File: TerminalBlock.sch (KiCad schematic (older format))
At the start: 2 parts, among them P4 12 Pin Terminal Block, P5 3 Pin TB

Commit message: Layout Work Session 14 Output
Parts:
- added C26, C27, C28, C29: C, SM1210, symbol C
- added R56: R, SM0805, symbol R
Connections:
- net +3.3V: now also C27.1
- net +5P: now also C26.1
- net GND_PWR: now also C26.2, C27.2, C28.2, C29.2, R56.1
- net TACH_IN: now also R56.2
- net V+_ADJ: now also C29.1
- net V-_ADJ: now also C28.1
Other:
- moved on the sheet: P4
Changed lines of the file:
@@
-EESchema Schematic File Version 2  date 11/21/2013 11:46:41 PM
+EESchema Schematic File Version 2  date 11/24/2013 3:13:43 PM
 LIBS:power
 LIBS:device
@@
 Sheet 7 9
 Title ""
-Date "22 nov 2013"
+Date "24 nov 2013"
 Rev ""
 Comp ""
@@
 RELAY_NC
 $Comp
-L +3.3V #PWR037
+L +3.3V #PWR43
 U 1 1 523FFDA7
 P 750 3500
-F 0 "#PWR037" H 750 3460 30  0001 C CNN
+F 0 "#PWR43" H 750 3460 30  0001 C CNN
 F 1 "+3.3V" H 750 3610 30  0000 C CNN
 F 2 "~" H 750 3500 60  0000 C CNN
@@
 L CONN_12 P4
 U 1 1 5258A829
-P 5850 1450
-F 0 "P4" V 5800 1450 60  0000 C CNN
-F 1 "12 Pin Terminal Block" V 5900 1450 60  0000 C CNN
-F 2 "" H 5850 1450 60  0000 C CNN
-F 3 "" H 5850 1450 60  0000 C CNN
-F 4 "On Shore" H 5850 1450 60  0001 C CNN "MFG Name"
-F 5 "OSTTE120104" H 5850 1450 60  0001 C CNN "MFG Part Number"
-	1    5850 1450
+P 8100 1450
+F 0 "P4" V 8050 1450 60  0000 C CNN
+F 1 "12 Pin Terminal Block" V 8150 1450 60  0000 C CNN
+F 2 "" H 8100 1450 60  0000 C CNN
+F 3 "" H 8100 1450 60  0000 C CNN
+F 4 "On Shore" H 8100 1450 60  0001 C CNN "MFG Name"
+F 5 "OSTTE120104" H 8100 1450 60  0001 C CNN "MFG Part Number"
+	1    8100 1450
 	1    0    0    -1
 $EndComp
@@
 	2050 1350 2050 1000
 Wire Wire Line
-	2050 1000 5500 1000
-Wire Wire Line
-	2200 1100 5500 1100
+	2050 1000 7750 1000
+Wire Wire Line
+	2200 1100 7750 1100
 Wire Wire Line
 	2200 1100 2200 2150
@@
 	2350 1200 2350 2325
 Wire Wire Line
-	2350 1200 5500 1200
-Wire Wire Line
-	5500 1300 2500 1300
+	2350 1200 7750 1200
+Wire Wire Line
+	7750 1300 2500 1300
 Wire Wire Line
 	2500 1300 2500 2600
@@
 	2700 2825 2700 1400
 Wire Wire Line
-	2700 1400 5500 1400
+	2700 1400 7750 1400
 Wire Wire Line
 	1800 3350 3000 3350
@@
 	2850 1500 2850 3000
 Wire Wire Line
-	2850 1500 5500 1500
-Wire Wire Line
-	5500 1600 3000 1600
+	2850 1500 7750 1500
+Wire Wire Line
+	7750 1600 3000 1600
 Wire Wire Line
 	3000 1600 3000 3350
@@
 	3200 3600 3200 1700
 Wire Wire Line
-	3200 1700 5500 1700
-Wire Wire Line
-	5500 1800 3400 1800
+	3200 1700 7750 1700
+Wire Wire Line
+	7750 1800 3400 1800
 Wire Wire Line
 	3400 1800 3400 4100
@@
 	3550 4400 3550 1900
 Wire Wire Line
-	3550 1900 5500 1900
-Wire Wire Line
-	5500 2000 3750 2000
+	3550 1900 7750 1900
+Wire Wire Line
+	7750 2000 3750 2000
 Wire Wire Line
 	3750 2000 3750 4550
@@
 	1825 2825 2700 2825
 Wire Wire Line
-	1450 900  5500 900
-$Comp
-L GND_PWR #PWR038
+	1450 900  7750 900
+$Comp
+L GND_PWR #PWR44
 U 1 1 527EF77D
 P 1000 3875
-F 0 "#PWR038" H 1000 3875 30  0001 C CNN
+F 0 "#PWR44" H 1000 3875 30  0001 C CNN
 F 1 "GND_PWR" H 1000 3805 30  0000 C CNN
 F 2 "~" H 1000 3875 60  0000 C CNN
@@
 	1    0    0    -1
 $EndComp
+$Comp
+L R R56
+U 1 1 52915224
+P 6300 2450
+F 0 "R56" V 6380 2450 40  0000 C CNN
+F 1 "R" V 6307 2451 40  0000 C CNN
+F 2 "SM0805" V 6230 2450 30  0000 C CNN
+F 3 "~" H 6300 2450 30  0000 C CNN
+	1    6300 2450
+	1    0    0    1
+$EndComp
+$Comp
+L GND_PWR #PWR46
+U 1 1 52915231
+P 5650 3450
+F 0 "#PWR46" H 5650 3450 30  0001 C CNN
+F 1 "GND_PWR" H 5650 3380 30  0000 C CNN
+F 2 "~" H 5650 3450 60  0000 C CNN
+F 3 "~" H 5650 3450 60  0000 C CNN
+	1    5650 3450
+	1    0    0    -1
+$EndComp
+Wire Wire Line
+	6300 3200 6300 2700
+$Comp
+L C C29
+U 1 1 52915CE9
+P 5600 2500
+F 0 "C29" H 5600 2600 40  0000 L CNN
+F 1 "C" H 5606 2415 40  0000 L CNN
+F 2 "SM1210" H 5638 2350 30  0000 C CNN
+F 3 "~" H 5600 2500 60  0000 C CNN
+	1    5600 2500
+	1    0    0    -1
+$EndComp
+Wire Wire Line
+	6300 2200 6300 1100
+Connection ~ 6300 1100
+Wire Wire Line
+	4500 3200 6300 3200
+Wire Wire Line
+	5650 3200 5650 3450
+Wire Wire Line
+	5600 2700 5600 3200
+Connection ~ 5650 3200
+$Comp
+L C C28
+U 1 1 52915E58
+P 5250 2500
+F 0 "C28" H 5250 2600 40  0000 L CNN
+F 1 "C" H 5256 2415 40  0000 L CNN
+F 2 "SM1210" H 5288 2350 30  0000 C CNN
+F 3 "~" H 5250 2500 60  0000 C CNN
+	1    5250 2500
+	1    0    0    -1
+$EndComp
+$Comp
+L C C27
+U 1 1 52915E5E
+P 4900 2500
+F 0 "C27" H 4900 2600 40  0000 L CNN
+F 1 "C" H 4906 2415 40  0000 L CNN
+F 2 "SM1210" H 4938 2350 30  0000 C CNN
+F 3 "~" H 4900 2500 60  0000 C CNN
+	1    4900 2500
+	1    0    0    -1
+$EndComp
+$Comp
+L C C26
+U 1 1 52915E6E
+P 4500 2500
+F 0 "C26" H 4500 2600 40  0000 L CNN
+F 1 "C" H 4506 2415 40  0000 L CNN
+F 2 "SM1210" H 4538 2350 30  0000 C CNN
+F 3 "~" H 4500 2500 60  0000 C CNN
+	1    4500 2500
+	1    0    0    -1
+$EndComp
+Wire Wire Line
+	4500 2700 4500 3200
+Connection ~ 5600 3200
+Wire Wire Line
+	5250 2700 5250 3200
+Connection ~ 5250 3200
+Wire Wire Line
+	4900 2700 4900 3200
+Connection ~ 4900 3200
+Wire Wire Line
+	5600 2300 5600 2000
+Connection ~ 5600 2000
+Wire Wire Line
+	5250 2300 5250 1900
+Connection ~ 5250 1900
+Wire Wire Line
+	4900 2300 4900 1800
+Connection ~ 4900 1800
+Wire Wire Line
+	4500 2300 4500 1600
+Connection ~ 4500 1600
 $EndSCHEMATC

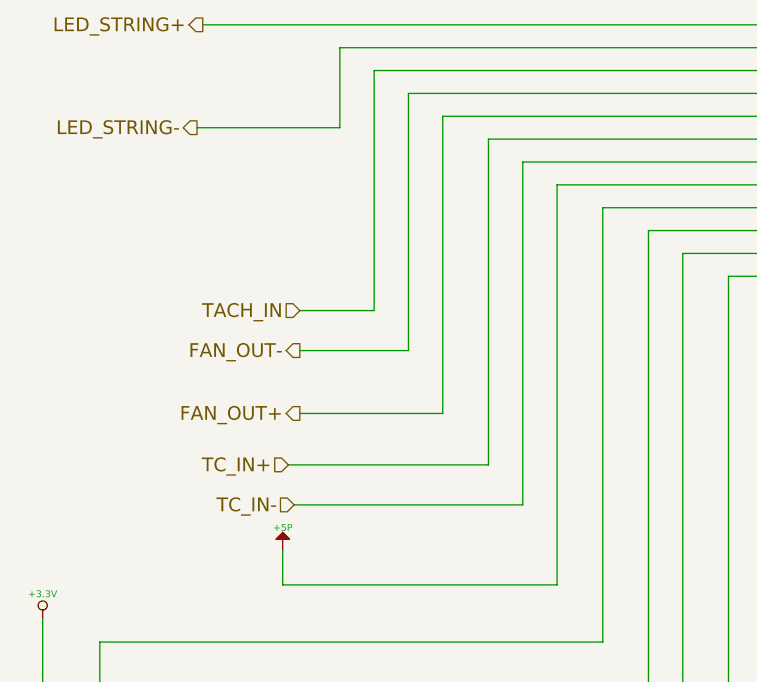
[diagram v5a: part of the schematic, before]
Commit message: Analog IO Cleanup/Additions
Added some placed holder caps and resistors
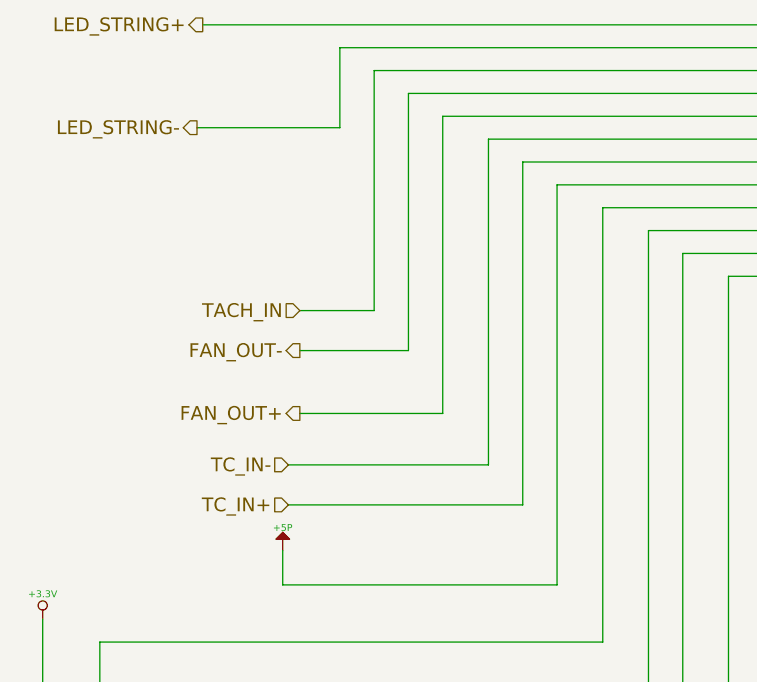
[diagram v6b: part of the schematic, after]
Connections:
- net TC_IN+: now also P4.7 (P7); no longer P4.6 (P6)
- net TC_IN-: now also P4.6 (P6); no longer P4.7 (P7)
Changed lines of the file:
@@
-EESchema Schematic File Version 2  date 12/18/2013 11:27:15 PM
+EESchema Schematic File Version 2  date 2/16/2014 3:41:32 PM
 LIBS:power
 LIBS:device
@@
 Sheet 7 9
 Title ""
-Date "19 dec 2013"
+Date "16 feb 2014"
 Rev ""
 Comp ""
@@
 Text HLabel 1425 1350 0    60   Output ~ 0
 LED_STRING-
+Text HLabel 1825 3000 0    60   Input ~ 0
+TC_IN+
 Text HLabel 1825 2825 0    60   Input ~ 0
-TC_IN+
-Text HLabel 1850 3000 0    60   Input ~ 0
 TC_IN-
 Text HLabel 2850 5500 0    60   BiDi ~ 0
@@
 RELAY_NC
 $Comp
-L +3.3V #PWR46
+L +3.3V #PWR040
 U 1 1 523FFDA7
 P 750 3500
-F 0 "#PWR46" H 750 3460 30  0001 C CNN
+F 0 "#PWR040" H 750 3460 30  0001 C CNN
 F 1 "+3.3V" H 750 3610 30  0000 C CNN
 F 2 "~" H 750 3500 60  0000 C CNN
@@
 	750  4100 3400 4100
 Wire Wire Line
-	2850 1500 2850 3000
+	2850 3000 2850 1500
 Wire Wire Line
 	2850 1500 7750 1500
@@
 	750  4100 750  3500
 Wire Wire Line
-	2850 3000 1850 3000
+	1825 3000 2850 3000
 Wire Wire Line
 	2350 2325 1875 2325
@@
 	1450 900  7750 900
 $Comp
-L GND_PWR #PWR47
+L GND_PWR #PWR041
 U 1 1 527EF77D
 P 1000 3875
-F 0 "#PWR47" H 1000 3875 30  0001 C CNN
+F 0 "#PWR041" H 1000 3875 30  0001 C CNN
 F 1 "GND_PWR" H 1000 3805 30  0000 C CNN
 F 2 "~" H 1000 3875 60  0000 C CNN
@@
 $EndComp
 $Comp
-L GND_PWR #PWR49
+L GND_PWR #PWR042
 U 1 1 52915231
 P 5650 3450
-F 0 "#PWR49" H 5650 3450 30  0001 C CNN
+F 0 "#PWR042" H 5650 3450 30  0001 C CNN
 F 1 "GND_PWR" H 5650 3380 30  0000 C CNN
 F 2 "~" H 5650 3450 60  0000 C CNN

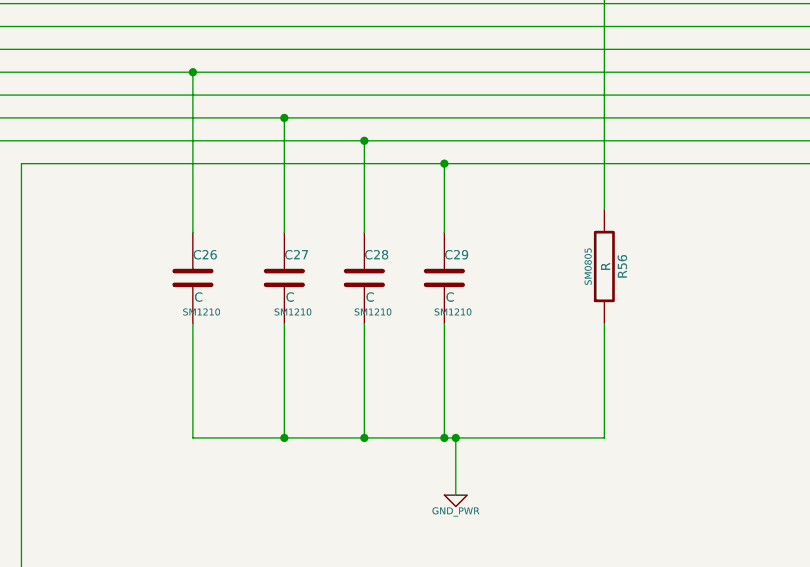
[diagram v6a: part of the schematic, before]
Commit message: Added Passive Values and SPICE models
As part of week 1 of Session 1B, we added a SPICE model of the In amp
and went through and assigned values to all of the passive components.
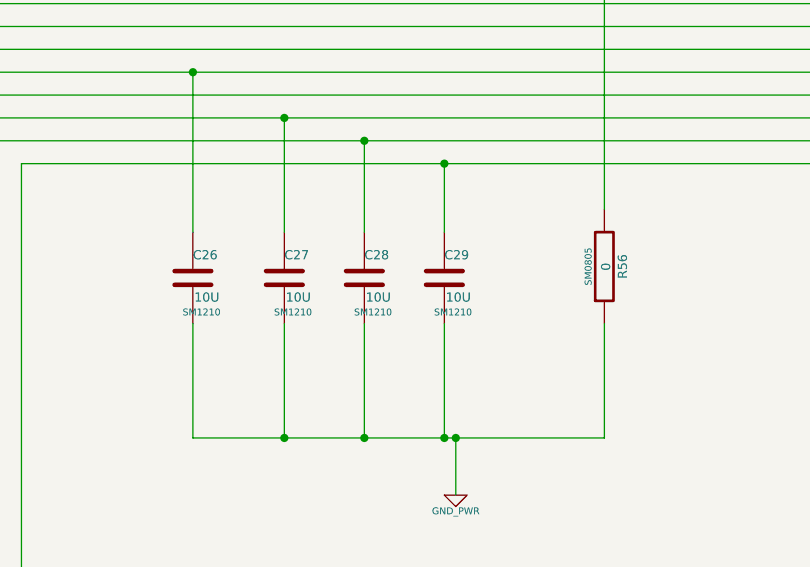
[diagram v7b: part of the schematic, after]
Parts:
- C26, C27, C28, C29: value C -> 10U
- R56: value R -> 0
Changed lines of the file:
@@
-EESchema Schematic File Version 2  date 2/16/2014 3:41:32 PM
+EESchema Schematic File Version 2  date 4/16/2014 11:04:06 PM
 LIBS:power
 LIBS:device
@@
 Sheet 7 9
 Title ""
-Date "16 feb 2014"
+Date "17 apr 2014"
 Rev ""
 Comp ""
@@
 P 6300 2450
 F 0 "R56" V 6380 2450 40  0000 C CNN
-F 1 "R" V 6307 2451 40  0000 C CNN
+F 1 "0" V 6307 2451 40  0000 C CNN
 F 2 "SM0805" V 6230 2450 30  0000 C CNN
 F 3 "~" H 6300 2450 30  0000 C CNN
@@
 P 5600 2500
 F 0 "C29" H 5600 2600 40  0000 L CNN
-F 1 "C" H 5606 2415 40  0000 L CNN
+F 1 "10U" H 5606 2415 40  0000 L CNN
 F 2 "SM1210" H 5638 2350 30  0000 C CNN
 F 3 "~" H 5600 2500 60  0000 C CNN
@@
 P 5250 2500
 F 0 "C28" H 5250 2600 40  0000 L CNN
-F 1 "C" H 5256 2415 40  0000 L CNN
+F 1 "10U" H 5256 2415 40  0000 L CNN
 F 2 "SM1210" H 5288 2350 30  0000 C CNN
 F 3 "~" H 5250 2500 60  0000 C CNN
@@
 P 4900 2500
 F 0 "C27" H 4900 2600 40  0000 L CNN
-F 1 "C" H 4906 2415 40  0000 L CNN
+F 1 "10U" H 4906 2415 40  0000 L CNN
 F 2 "SM1210" H 4938 2350 30  0000 C CNN
 F 3 "~" H 4900 2500 60  0000 C CNN
@@
 P 4500 2500
 F 0 "C26" H 4500 2600 40  0000 L CNN
-F 1 "C" H 4506 2415 40  0000 L CNN
+F 1 "10U" H 4506 2415 40  0000 L CNN
 F 2 "SM1210" H 4538 2350 30  0000 C CNN
 F 3 "~" H 4500 2500 60  0000 C CNN

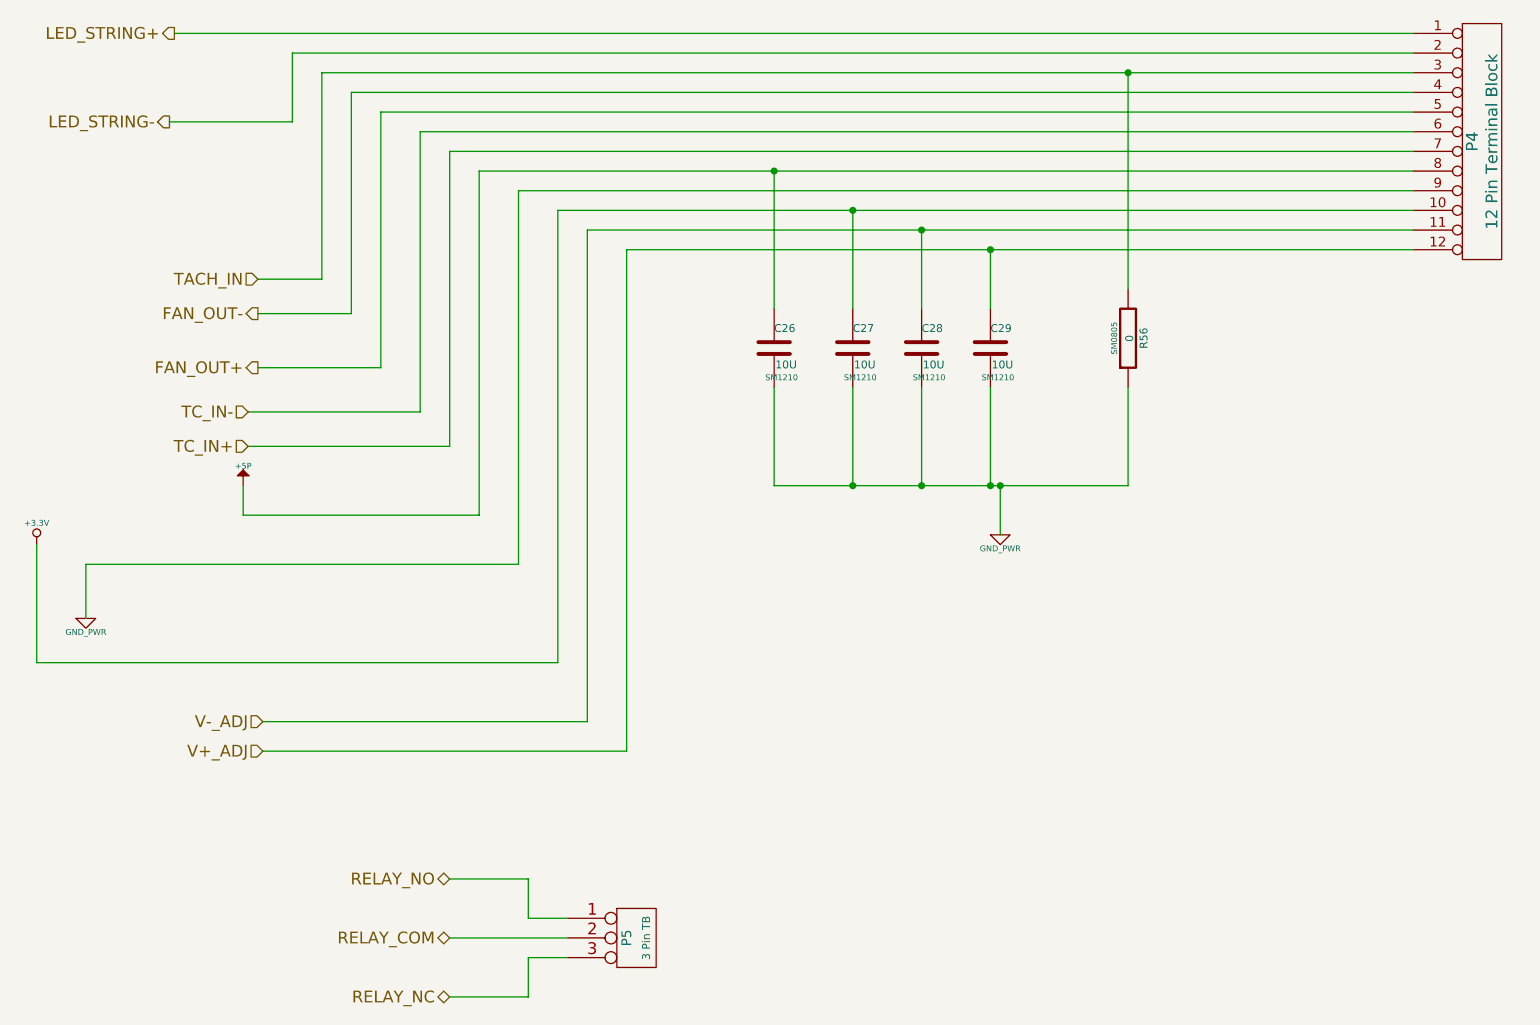
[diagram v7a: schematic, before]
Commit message: Added the schematic and BOM changes back in after hard reset
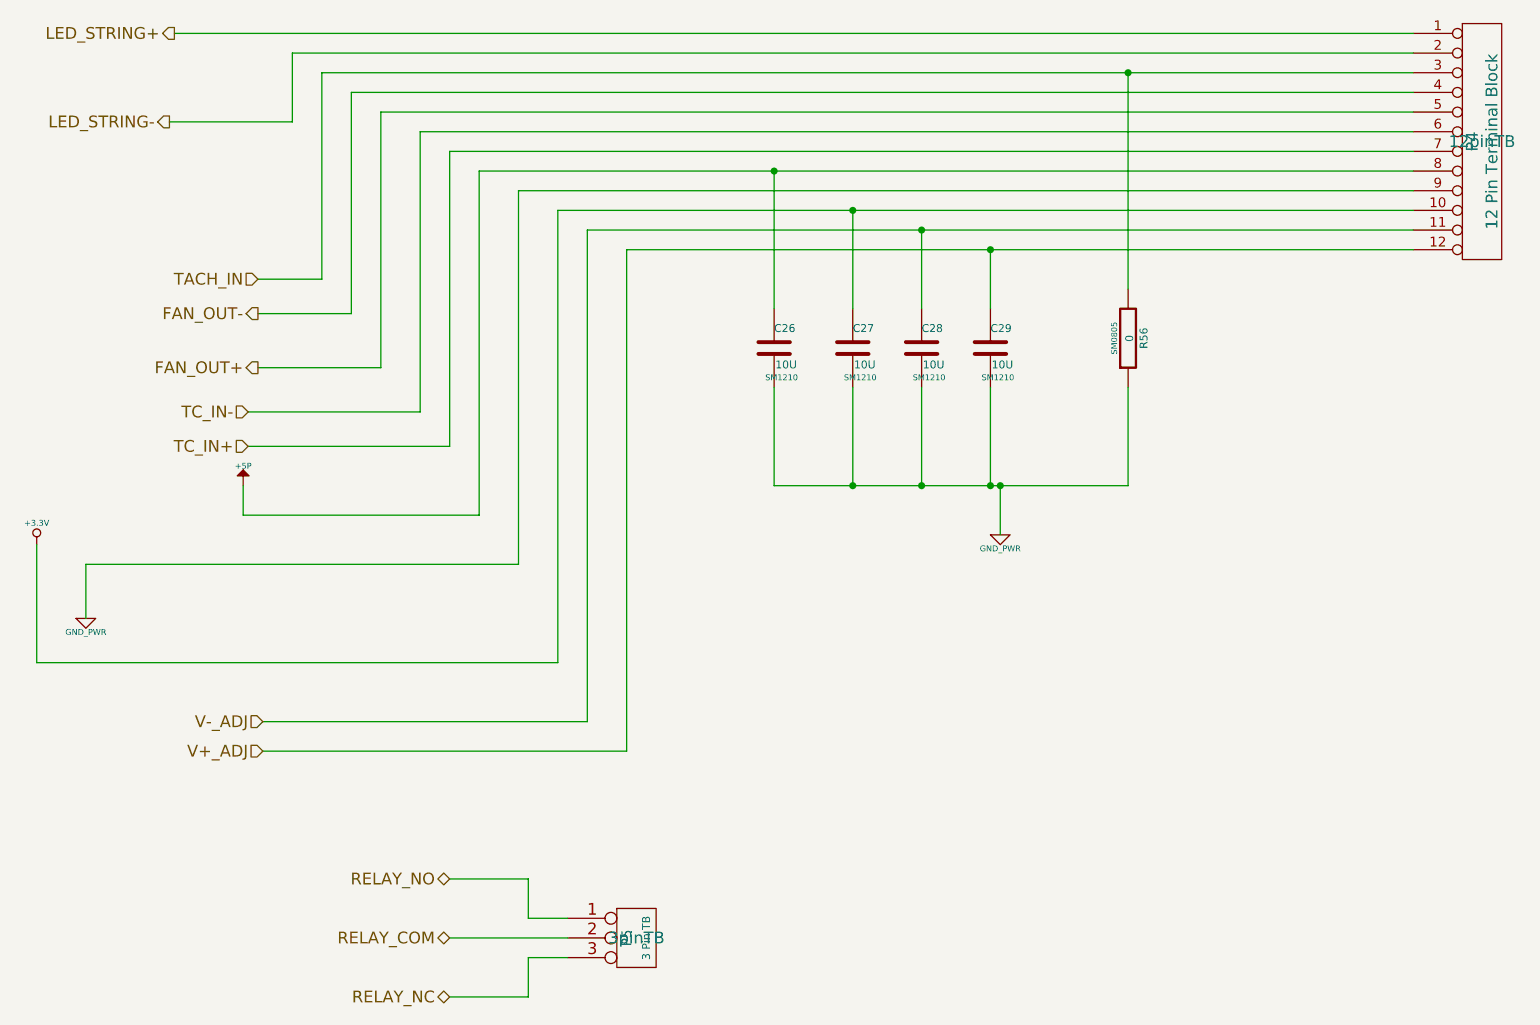
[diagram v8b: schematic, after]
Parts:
- P4: footprint (none) -> 12pinTB
- P5: footprint (none) -> 3pinTB
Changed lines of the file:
@@
-EESchema Schematic File Version 2  date 4/16/2014 11:04:06 PM
+EESchema Schematic File Version 2  date 4/18/2014 9:49:53 PM
 LIBS:power
 LIBS:device
@@
 Sheet 7 9
 Title ""
-Date "17 apr 2014"
+Date "19 apr 2014"
 Rev ""
 Comp ""
@@
 F 0 "P4" V 8050 1450 60  0000 C CNN
 F 1 "12 Pin Terminal Block" V 8150 1450 60  0000 C CNN
-F 2 "" H 8100 1450 60  0000 C CNN
+F 2 "12pinTB" H 8100 1450 60  0000 C CNN
 F 3 "" H 8100 1450 60  0000 C CNN
 F 4 "On Shore" H 8100 1450 60  0001 C CNN "MFG Name"
@@
 F 0 "P5" V 3750 5500 50  0000 C CNN
 F 1 "3 Pin TB" V 3850 5500 40  0000 C CNN
-F 2 "" H 3800 5500 60  0000 C CNN
+F 2 "3pinTB" H 3800 5500 60  0000 C CNN
 F 3 "" H 3800 5500 60  0000 C CNN
 F 4 "Phoenix" H 3800 5500 60  0001 C CNN "MFG Name"
